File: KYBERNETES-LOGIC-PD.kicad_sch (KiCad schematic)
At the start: 33 parts, among them J1 Logic Battery, J10 Battery Low, J2 Regulator In, J3 Regulator Out, J4 I2C, J4 Regulator Enable, J6 USB_C_Receptacle_PowerOnly_6P, J7 USB_C_Receptacle_PowerOnly_6P, J8 USB_C_Receptacle_PowerOnly_6P, J9 USB_C_Receptacle_PowerOnly_6P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

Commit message: derp
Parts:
- H1, H2, H3, H4: footprint MountingHole:MountingHole_3.2mm_M3_DIN965_Pad -> Footprints:MountingHole_3.2mm_M3_Pad_Square
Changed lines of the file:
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@@
       (effects (font (size 1.27 1.27)) (justify left))
     )
-    (property "Footprint" "MountingHole:MountingHole_3.2mm_M3_DIN965_Pad" (at 144.145 175.26 0)
+    (property "Footprint" "Footprints:MountingHole_3.2mm_M3_Pad_Square" (at 144.145 175.26 0)
       (effects (font (size 1.27 1.27)) hide)
     )
@@
       (effects (font (size 1.27 1.27)) (justify left))
     )
-    (property "Footprint" "MountingHole:MountingHole_3.2mm_M3_DIN965_Pad" (at 120.015 161.925 0)
+    (property "Footprint" "Footprints:MountingHole_3.2mm_M3_Pad_Square" (at 120.015 161.925 0)
       (effects (font (size 1.27 1.27)) hide)
     )
@@
       (effects (font (size 1.27 1.27)) (justify left))
     )
-    (property "Footprint" "MountingHole:MountingHole_3.2mm_M3_DIN965_Pad" (at 120.015 175.26 0)
+    (property "Footprint" "Footprints:MountingHole_3.2mm_M3_Pad_Square" (at 120.015 175.26 0)
       (effects (font (size 1.27 1.27)) hide)
     )
@@
       (effects (font (size 1.27 1.27)) (justify left))
     )
-    (property "Footprint" "MountingHole:MountingHole_3.2mm_M3_DIN965_Pad" (at 144.145 161.925 0)
-      (effects (font (size 1.27 1.27)) hide)
-    )
+    (property "Footprint" "Footprints:MountingHole_3.2mm_M3_Pad_Square" (at 144.145 161.925 0)
+      (effects (font (size 1.27 1.27)) hide)
+    )

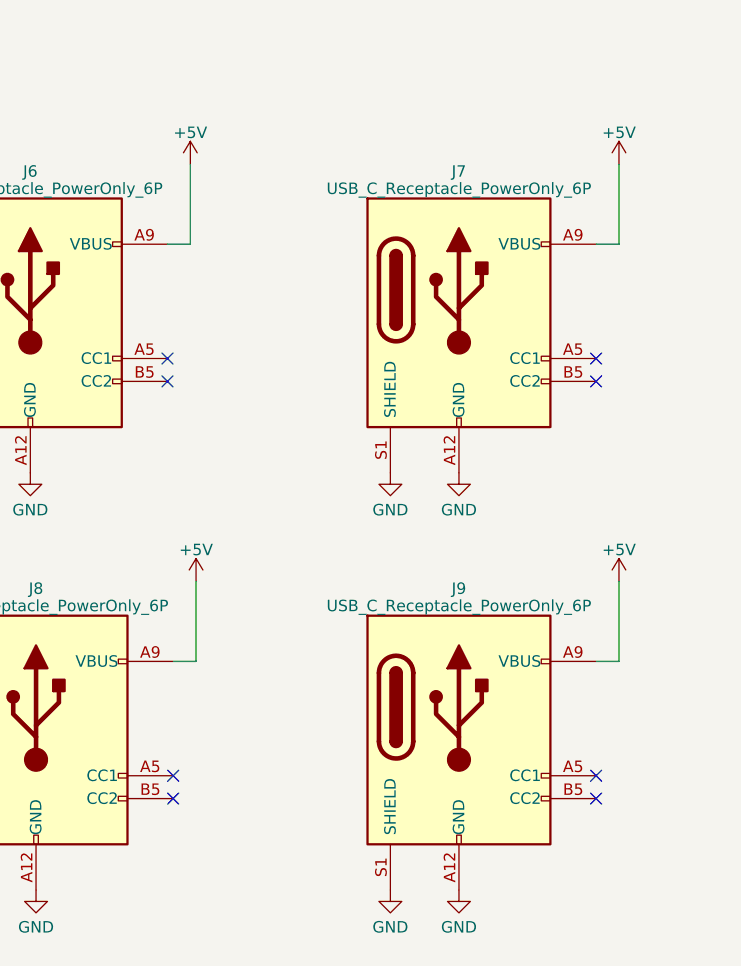
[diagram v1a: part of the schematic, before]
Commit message: source needs 10 Kohm pullups to advertise 3A capability
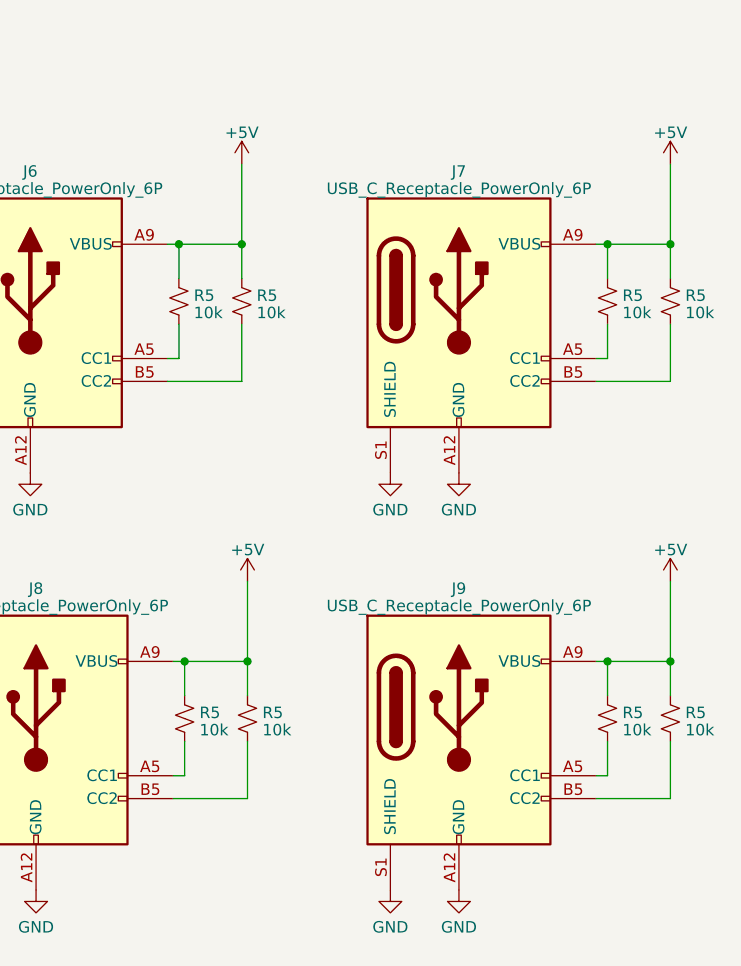
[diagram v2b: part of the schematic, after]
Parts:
- added R5 (x8): 10k, Resistor_SMD:R_0603_1608Metric_Pad0.98x0.95mm_HandSolder, symbol Device:R_Small_US
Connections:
- net +5V: now also R5.1, R5.1, R5.1, R5.1, R5.1, R5.1, R5.1, R5.1
- net at J6.A5 (CC1): now also R5.2
- net at J6.B5 (CC2): now also R5.2
- net at J8.A5 (CC1): now also R5.2
- net at J8.B5 (CC2): now also R5.2
- net at J7.A5 (CC1): now also R5.2
- net at J7.B5 (CC2): now also R5.2
- net at J9.A5 (CC1): now also R5.2
- net at J9.B5 (CC2): now also R5.2
- no-connect marks 9 -> 1
